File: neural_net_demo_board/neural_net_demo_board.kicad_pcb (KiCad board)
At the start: 2 copper layers, 11 parts, among them U1 XIAO-RP2040-DIP, U2 TMP36GRTZ-REEL7, U3 TEMT6000X01

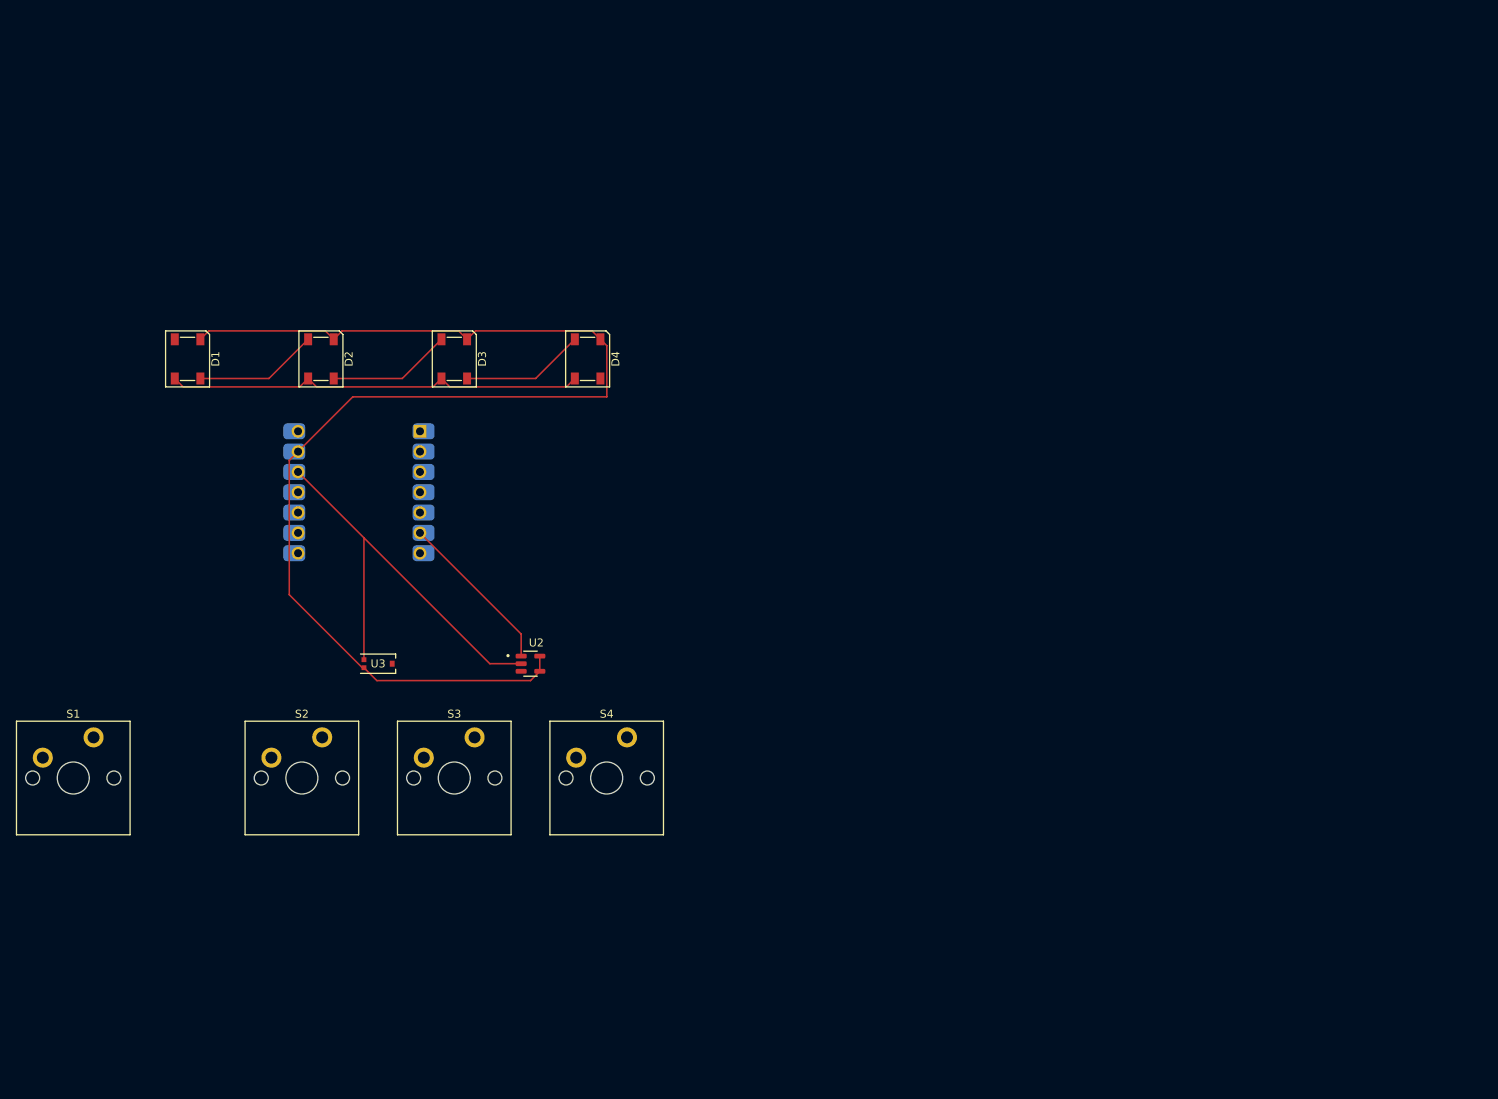
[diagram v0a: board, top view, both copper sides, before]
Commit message: Integrate rp2040, input/outputs
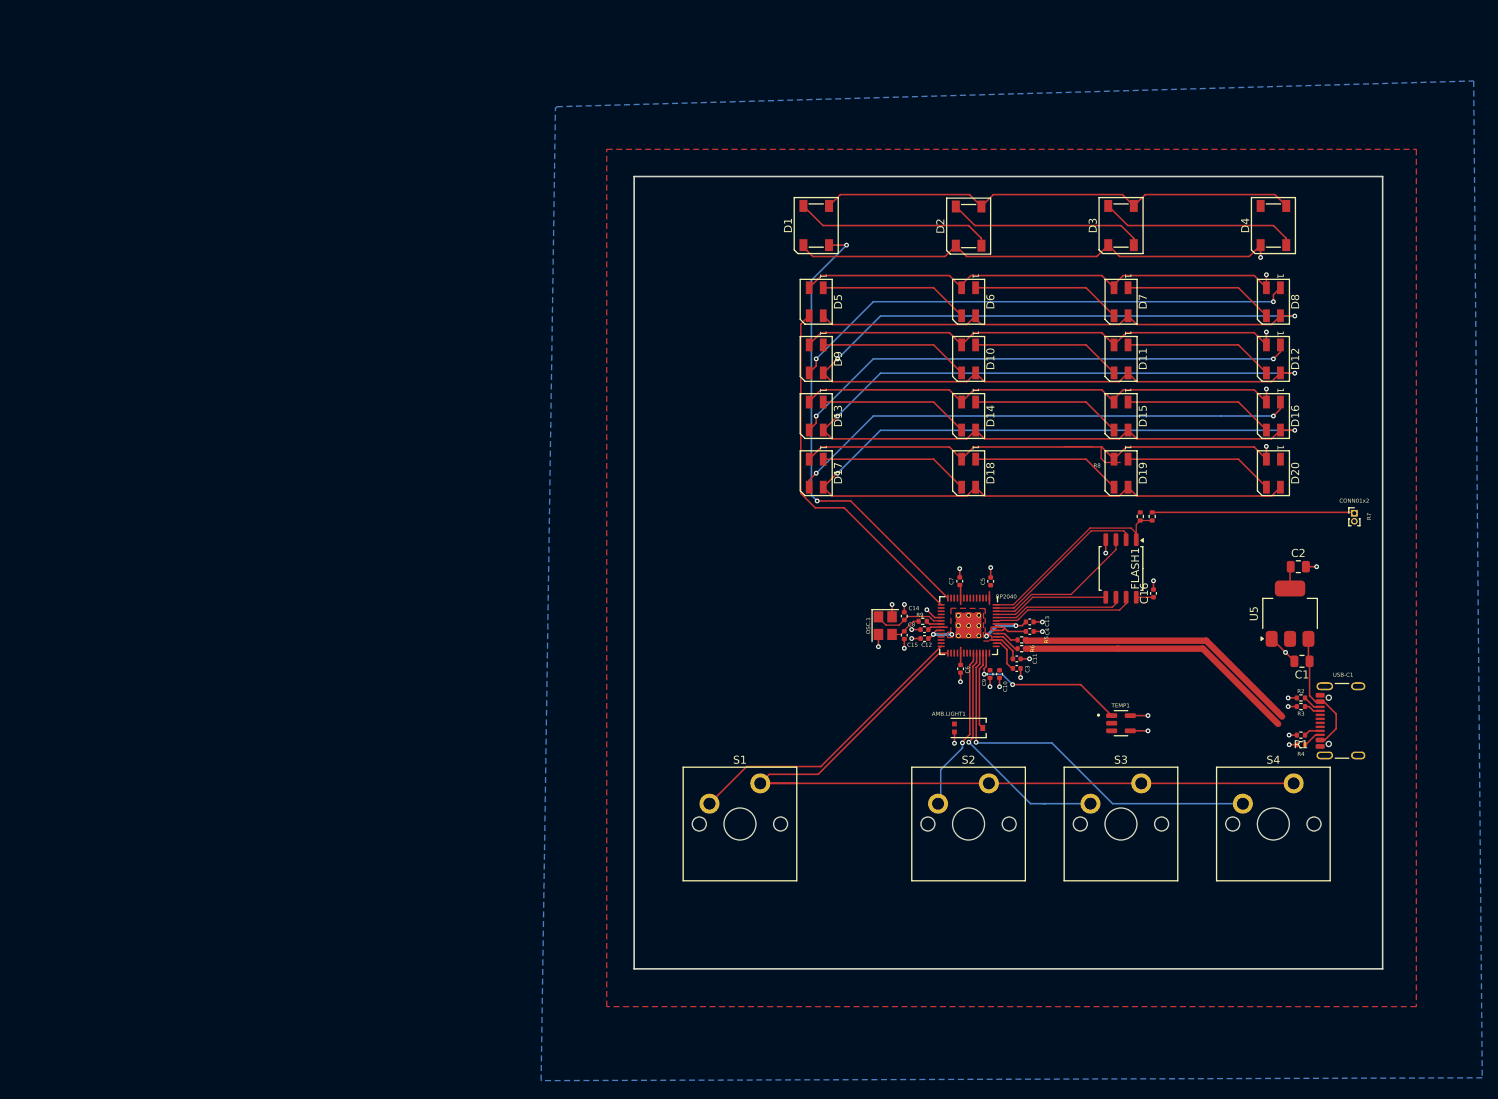
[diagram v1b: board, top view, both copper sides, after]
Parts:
- removed U1: XIAO-RP2040-DIP, ScottoKeebs_MCU:Seeed_XIAO_RP2040
- removed U2: TMP36GRTZ-REEL7, TMP36GRTZ_REEL7(1):SOT95P280X145-5N
- removed U3: TEMT6000X01, footprints:SMT_6000X01_VIS
- added AMB.LIGHT1: TEMT6000X01, footprints:SMT_6000X01_VIS, F.Cu at (188.1, 108.0)
- added C1: 10u, Capacitor_SMD:C_0805_2012Metric, F.Cu at (229.8, 99.7)
- added C10: 100n, Capacitor_SMD:C_0402_1005Metric, F.Cu at (192.0, 101.3)
- added C11: 1u, Capacitor_SMD:C_0402_1005Metric, F.Cu at (194.1, 99.4)
- added C12: 100n, Capacitor_SMD:C_0402_1005Metric, F.Cu at (182.6, 96.9)
- added C13: 100n, Capacitor_SMD:C_0402_1005Metric, F.Cu at (195.8, 94.8)
- added C14: 15p, Capacitor_SMD:C_0402_1005Metric, F.Cu at (180.1, 94.1)
- added C15: 15p, Capacitor_SMD:C_0402_1005Metric, F.Cu at (180.1, 96.4)
- added C16: 100n, Capacitor_SMD:C_0402_1005Metric, F.Cu at (211.2, 91.2)
- added C2: 10u, Capacitor_SMD:C_0805_2012Metric, F.Cu at (229.3, 87.9)
- added C3: 1u, Capacitor_SMD:C_0402_1005Metric, F.Cu at (194.1, 100.6)
- added C4: 100n, Capacitor_SMD:C_0402_1005Metric, F.Cu at (195.8, 96.0)
- added C5: 100n, Capacitor_SMD:C_0402_1005Metric, F.Cu at (190.9, 89.7)
- added C6: 100n, Capacitor_SMD:C_0402_1005Metric, F.Cu at (187.1, 100.7)
- added C7: 100n, Capacitor_SMD:C_0402_1005Metric, F.Cu at (187.0, 89.7)
- added C8: 100n, Capacitor_SMD:C_0402_1005Metric, F.Cu at (182.6, 95.8)
- added C9: 100n, Capacitor_SMD:C_0402_1005Metric, F.Cu at (190.8, 101.3)
- added CONN01x2: Conn_01x02 USB_BOOT, Connector_PinHeader_1.00mm:PinHeader_1x02_P1.00mm_Vertical, F.Cu at (236.3, 81.2)
- added D10: SK6812MINI, LED_SMD:LED_SK6812MINI_PLCC4_3.5x3.5mm_P1.75mm, F.Cu at (188.1, 61.9)
- added D11: SK6812MINI, LED_SMD:LED_SK6812MINI_PLCC4_3.5x3.5mm_P1.75mm, F.Cu at (207.2, 61.9)
- added D12: SK6812MINI, LED_SMD:LED_SK6812MINI_PLCC4_3.5x3.5mm_P1.75mm, F.Cu at (226.2, 61.9)
- added D13: SK6812MINI, LED_SMD:LED_SK6812MINI_PLCC4_3.5x3.5mm_P1.75mm, F.Cu at (169.1, 69.1)
- added D14: SK6812MINI, LED_SMD:LED_SK6812MINI_PLCC4_3.5x3.5mm_P1.75mm, F.Cu at (188.1, 69.1)
- added D15: SK6812MINI, LED_SMD:LED_SK6812MINI_PLCC4_3.5x3.5mm_P1.75mm, F.Cu at (207.2, 69.1)
- added D16: SK6812MINI, LED_SMD:LED_SK6812MINI_PLCC4_3.5x3.5mm_P1.75mm, F.Cu at (226.2, 69.1)
- added D17: SK6812MINI, LED_SMD:LED_SK6812MINI_PLCC4_3.5x3.5mm_P1.75mm, F.Cu at (169.1, 76.2)
- added D18: SK6812MINI, LED_SMD:LED_SK6812MINI_PLCC4_3.5x3.5mm_P1.75mm, F.Cu at (188.1, 76.2)
- added D19: SK6812MINI, LED_SMD:LED_SK6812MINI_PLCC4_3.5x3.5mm_P1.75mm, F.Cu at (207.2, 76.2)
- added D20: SK6812MINI, LED_SMD:LED_SK6812MINI_PLCC4_3.5x3.5mm_P1.75mm, F.Cu at (226.2, 76.2)
- added D5: SK6812MINI, LED_SMD:LED_SK6812MINI_PLCC4_3.5x3.5mm_P1.75mm, F.Cu at (169.1, 54.8)
- added D6: SK6812MINI, LED_SMD:LED_SK6812MINI_PLCC4_3.5x3.5mm_P1.75mm, F.Cu at (188.1, 54.8)
- added D7: SK6812MINI, LED_SMD:LED_SK6812MINI_PLCC4_3.5x3.5mm_P1.75mm, F.Cu at (207.2, 54.8)
- added D8: SK6812MINI, LED_SMD:LED_SK6812MINI_PLCC4_3.5x3.5mm_P1.75mm, F.Cu at (226.2, 54.8)
- added D9: SK6812MINI, LED_SMD:LED_SK6812MINI_PLCC4_3.5x3.5mm_P1.75mm, F.Cu at (169.1, 61.9)
- added FLASH1: W25Q128JVS, Package_SO:SOIC-8_5.23x5.23mm_P1.27mm, F.Cu at (207.2, 88.1)
- added OSC.1: ABM8-272-T3, Crystal:Crystal_SMD_3225-4Pin_3.2x2.5mm, F.Cu at (177.7, 95.3)
- added R1: 5.1 kΩ, Resistor_SMD:R_0402_1005Metric, F.Cu at (229.7, 108.9)
- added R2: 5.1 kΩ, Resistor_SMD:R_0402_1005Metric, F.Cu at (229.7, 104.3)
- added R3: 1 MΩ, Resistor_SMD:R_0402_1005Metric, F.Cu at (229.7, 105.4)
- added R4: 1 MΩ, Resistor_SMD:R_0402_1005Metric, F.Cu at (229.7, 110.1)
- added R5: 27 Ω, Resistor_SMD:R_0402_1005Metric, F.Cu at (194.8, 97.0)
- added R6: 27 Ω, Resistor_SMD:R_0402_1005Metric, F.Cu at (194.8, 98.1)
- added R7: 1 kΩ, Resistor_SMD:R_0402_1005Metric, F.Cu at (211.1, 81.6)
- added R8: DO NOT FIT, Resistor_SMD:R_0402_1005Metric, F.Cu at (209.6, 81.6)
- added R9: 1 kΩ, Resistor_SMD:R_0402_1005Metric, F.Cu at (182.4, 94.7)
- added RP2040: MCU_RaspberryPi_RP2040_RP2040, RP2040_minimal_r2:RP2040-QFN-56, F.Cu at (188.1, 95.2)
- added TEMP1: TMP36GRTZ-REEL7, TMP36GRTZ_REEL7(1):SOT95P280X145-5N, F.Cu at (207.2, 107.5)
- added U5: NCP1117-3.3_SOT223, Package_TO_SOT_SMD:SOT-223-3_TabPin2, F.Cu at (228.3, 93.8)
- added USB-C1: USB_C_Receptacle_USB2.0_16P, Connector_USB:USB_C_Receptacle_GCT_USB4105-xx-A_16P_TopMnt_Horizontal, F.Cu at (235.7, 107.2)
- moved D4 87.3 mm to (226.2, 45.2), turned to 90 degrees
- moved D3 85.0 mm to (207.2, 45.2), turned to 90 degrees
- moved S2 83.5 mm to (188.1, 120.0)
- moved S4 83.5 mm to (226.2, 120.0)
- moved S1 83.5 mm to (159.5, 120.0)
- moved S3 83.5 mm to (207.2, 120.0)
- moved D2 82.6 mm to (188.1, 45.3), turned to 90 degrees
- moved D1 80.3 mm to (169.1, 45.2), turned to 90 degrees
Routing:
- net +3.3V: track 105.7 -> 516.5 mm, vias 0 -> 6
- net GND: track 158.1 -> 358.9 mm, vias 0 -> 32
- net ROW 1: track 0.00 -> 102.1 mm
- net Net-(D8-DOUT): track 0.00 -> 64.3 mm, vias 0 -> 2
- net Net-(D16-DOUT): track 0.00 -> 64.3 mm, vias 0 -> 2
- net Net-(D12-DOUT): track 0.00 -> 64.3 mm, vias 0 -> 2
- net RGB: track 0.00 -> 57.7 mm, vias 0 -> 2
- net COL 4: track 0.00 -> 47.9 mm, vias 0 -> 1
- net RGB2: track 0.00 -> 45.9 mm
- net COL 1: track 0.00 -> 37.2 mm
- net USBD+: track 0.00 -> 36.0 mm
- net USBD-: track 0.00 -> 35.6 mm
- net COL 3: track 0.00 -> 29.9 mm, vias 0 -> 1
- net QSPI_SS: track 0.00 -> 26.7 mm
- net Net-(CONN01x2-Pin_1): track 0.00 -> 25.2 mm
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- added copper zone on F.Cu, net +1V1
- added copper zone on F.Cu, net +3.3V
- added copper zone on B.Cu, net GND
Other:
- board outline added: 93.6 x 99 mm
- board text added: "R8"

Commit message: pcb's basically done atp
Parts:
- added C17: 10u, Capacitor_SMD:C_0805_2012Metric, F.Cu at (215.8, 84.5)
- added CONN01x24: Conn_01x24, Connector_PinHeader_1.00mm:PinHeader_1x24_P1.00mm_Vertical, F.Cu at (148.8, 85.5)
- added G***: LOGO, LOGO, F.Cu at (153.9, 59.5)
- added G***: LOGO, LOGO, B.Cu at (202.7, 95.3)
- added G***: LOGO, LOGO, F.Cu at (153.9, 44.6)
- added G***: LOGO, LOGO, F.Cu at (153.9, 52.4)
- added G***: LOGO, LOGO, F.Cu at (165.8, 95.2)
- added G***: LOGO, LOGO, F.Cu at (207.2, 88.1)
- added G***: LOGO, LOGO, B.Cu at (189.8, 95.0)
- added G***: LOGO, LOGO, B.Cu at (188.1, 95.2)
- added G***: LOGO, LOGO, B.Cu at (175.6, 103.1)
- added G***: LOGO, LOGO, B.Cu at (173.8, 120.8)
- USB-C1: moved to B.Cu
- moved R2 6.12 mm to (228.8, 110.4)
- moved R4 5.96 mm to (228.2, 104.3)
- moved R3 4.00 mm to (228.8, 109.3)
- moved R1 3.69 mm to (228.2, 105.5)
- moved C3 1.18 mm to (194.0, 99.4)
- moved C13 1.13 mm to (195.0, 94.0)
- moved C4 1.13 mm to (195.0, 95.1)
- moved C11 1.07 mm to (194.4, 98.4)
- moved C12 1.01 mm to (181.6, 96.8)
- moved C6 0.97 mm to (186.5, 101.4)
- moved R5 0.83 mm to (194.7, 96.2)
- moved R6 0.83 mm to (194.7, 97.3)
- moved C10 0.61 mm to (192.5, 101.0)
- moved C9 0.61 mm to (191.3, 101.0)
- moved C8 0.56 mm to (182.1, 95.6)
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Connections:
- RP2040 pad 11: unconnected-(RP2040-GPIO8-Pad11) -> GP2
- RP2040 pad 12: unconnected-(RP2040-GPIO9-Pad12) -> GP1
- RP2040 pad 13: unconnected-(RP2040-GPIO10-Pad13) -> GP0
- RP2040 pad 16: unconnected-(RP2040-GPIO13-Pad16) -> GP13
- RP2040 pad 17: unconnected-(RP2040-GPIO14-Pad17) -> GP14
- RP2040 pad 18: unconnected-(RP2040-GPIO15-Pad18) -> GP15
- RP2040 pad 2: unconnected-(RP2040-GPIO0-Pad2) -> GP10
- RP2040 pad 24: unconnected-(RP2040-SWCLK-Pad24) -> SWCLK
- RP2040 pad 25: unconnected-(RP2040-SWD-Pad25) -> SWD
- RP2040 pad 26: unconnected-(RP2040-RUN-Pad26) -> RUN
- RP2040 pad 27: unconnected-(RP2040-GPIO16-Pad27) -> GP16
- RP2040 pad 3: unconnected-(RP2040-GPIO1-Pad3) -> GP9
- RP2040 pad 30: unconnected-(RP2040-GPIO19-Pad30) -> GP19
- RP2040 pad 31: unconnected-(RP2040-GPIO20-Pad31) -> GP20
- RP2040 pad 32: unconnected-(RP2040-GPIO21-Pad32) -> GP21
- RP2040 pad 34: unconnected-(RP2040-GPIO22-Pad34) -> GP22
- RP2040 pad 35: unconnected-(RP2040-GPIO23-Pad35) -> GP23
- RP2040 pad 36: unconnected-(RP2040-GPIO24-Pad36) -> GP24
- RP2040 pad 4: unconnected-(RP2040-GPIO2-Pad4) -> GP8
- RP2040 pad 5: unconnected-(RP2040-GPIO3-Pad5) -> GP7
- RP2040 pad 6: unconnected-(RP2040-GPIO4-Pad6) -> GP6
- RP2040 pad 7: unconnected-(RP2040-GPIO5-Pad7) -> GP5
- RP2040 pad 8: unconnected-(RP2040-GPIO6-Pad8) -> GP4
- RP2040 pad 9: unconnected-(RP2040-GPIO7-Pad9) -> GP3
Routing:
- net GP8: track 0.00 -> 48.9 mm
- net GP9: track 0.00 -> 48.7 mm
- net GP10: track 0.00 -> 48.5 mm
- net GP7: track 0.00 -> 47.5 mm
- net GP6: track 0.00 -> 47.2 mm
- net GP5: track 0.00 -> 47.0 mm
- net GP4: track 0.00 -> 46.6 mm
- net GP3: track 0.00 -> 46.3 mm
- net GP24: track 0.00 -> 45.8 mm
- net GP23: track 0.00 -> 45.4 mm
- net GP22: track 0.00 -> 45.0 mm
- net GP21: track 0.00 -> 42.7 mm
- net GP20: track 0.00 -> 42.3 mm
- net GP19: track 0.00 -> 41.9 mm
- net GP2: track 0.00 -> 41.8 mm
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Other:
- board text added: "05.16.2025 1747411200"
- board text added: "Built on RP2040 Powered by MicroPython Trained with TensorFlow"
- board text added: "GPIO 10 GPIO 9 GPIO 8 GPIO 7 GPIO 6 GPIO 5 GPIO 4 GPIO 3 GPIO 2 GPIO 1 GPIO 0 GPIO 13 GPIO 14 GPIO 15 SWCLK SWD RUN GPIO 16 GPIO 19 GPIO 20 GPIO 21 GPIO 22 GPIO 23 GPIO 24"
- board text added: "IMF-04051996-CLASSIFIED"
- board text added: "JLCJLCJLCJLC"
- board text added: "github.com/sidsenthilexe/neural-net-demo-board"

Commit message: starting to learn tensorflow
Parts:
- moved G*** 0.21 mm to (202.7, 95.5)
